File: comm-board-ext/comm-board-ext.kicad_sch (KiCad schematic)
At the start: 39 parts, among them J1 GND, J10 MCU-RxD1, J11 MCU-TxD2, J12 MCU-RxD2, J2 GND, J3 +5V, J4 +3.3V, J5 D1-, J6 D1+, J7 D2+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

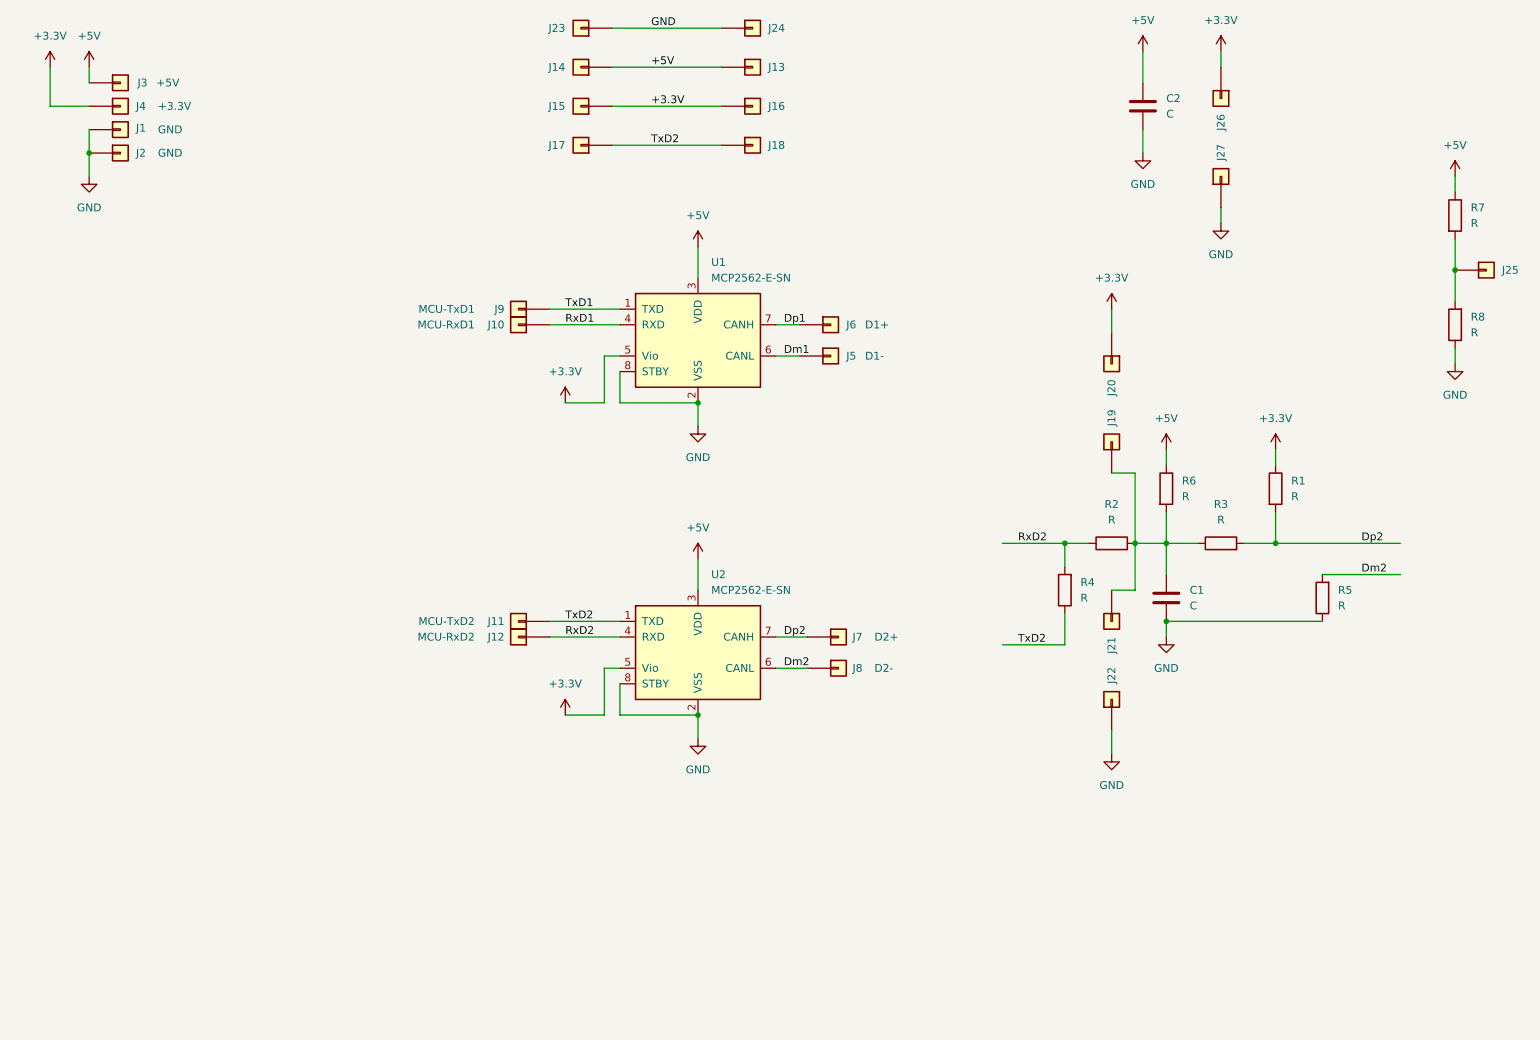
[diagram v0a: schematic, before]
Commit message: comm-board-ext: Modified for CNC milling
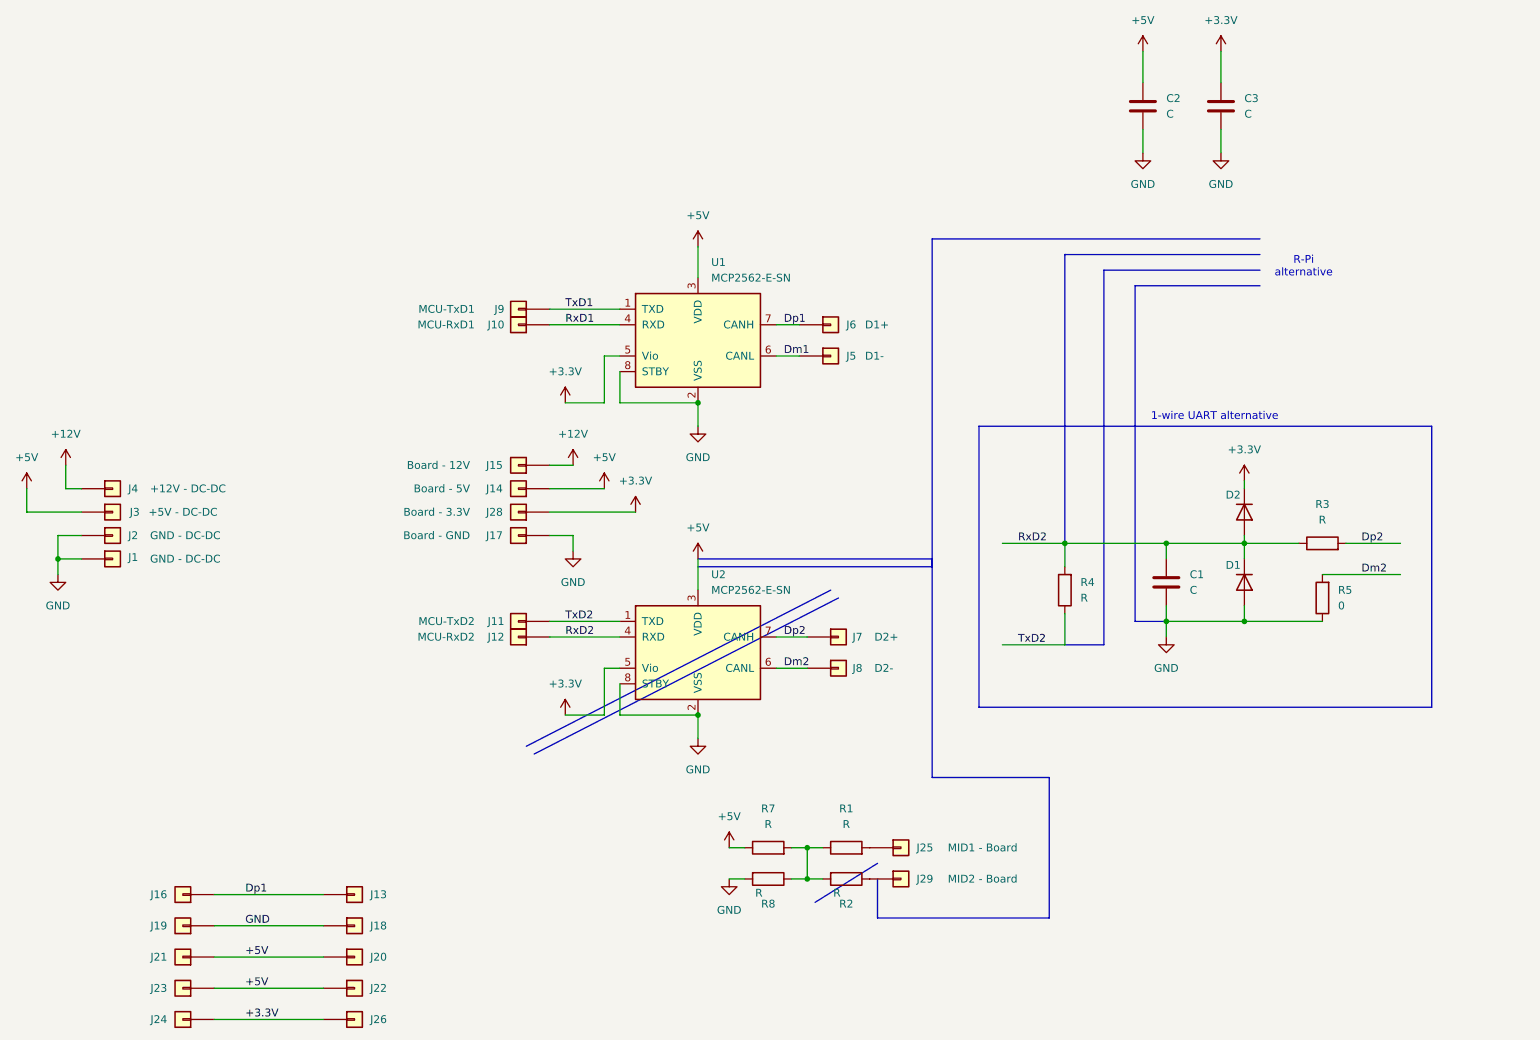
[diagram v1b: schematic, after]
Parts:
- removed J27: ~, Footprints:VHDR, symbol Connector_Generic:Conn_01x01
- removed R6: R, Resistor_SMD:R_1206_3216Metric_Pad1.30x1.75mm_HandSolder, symbol Device:R
- added C3: C, Footprints:CNC-mill-0.7-CAP, symbol Device:C
- added D1, D2: D, Footprints:CNC-mill-0.7-RES, symbol Device:D
- added J28: Board - 3.3V, Footprints:CHDR, symbol Connector_Generic:Conn_01x01
- added J29: MID2 - Board, Footprints:CHDR, symbol Connector_Generic:Conn_01x01
- C1, C2: footprint Resistor_SMD:R_1206_3216Metric_Pad1.30x1.75mm_HandSolder -> Footprints:CNC-mill-0.7-CAP
- J1, J2: value GND -> GND - DC-DC; footprint Footprints:BBHDR -> Footprints:CHDR
- J10, J11, J12, J5, J6, J7, J8, J9: footprint Footprints:BBHDR -> Footprints:CHDR
- J14: value ~ -> Board - 5V; footprint Footprints:VHDR -> Footprints:CHDR
- J15: value ~ -> Board - 12V; footprint Footprints:VHDR -> Footprints:CHDR
- J17: value ~ -> Board - GND; footprint Footprints:VHDR -> Footprints:CHDR
- J19, J20, J21, J22: footprint Footprints:CHDR -> Footprints:VHDR
- J25: value ~ -> MID1 - Board; footprint Footprints:VHDR -> Footprints:CHDR
- J3: value +5V -> +5V - DC-DC; footprint Footprints:BBHDR -> Footprints:CHDR
- J4: value +3.3V -> +12V - DC-DC; footprint Footprints:BBHDR -> Footprints:CHDR
- R1, R2, R3, R4, R7, R8: footprint Resistor_SMD:R_1206_3216Metric_Pad1.30x1.75mm_HandSolder -> Footprints:CNC-mill-0.7-RES
- R5: value R -> 0; footprint Resistor_SMD:R_1206_3216Metric_Pad1.30x1.75mm_HandSolder -> Footprints:CNC-mill-0.7-RES
- U1, U2: footprint Package_SO:SOIC-8_3.9x4.9mm_P1.27mm -> Footprints:CNC-mill-0.7-DIP-8
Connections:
- net +3.3V: now also J24.1 (Pin_1), C3.1, D2.1 (K), J28.1 (Pin_1); no longer J15.1 (Pin_1), J16.1 (Pin_1), J20.1 (Pin_1), J4.1 (Pin_1), R1.1
- net +5V: now also J20.1 (Pin_1), J21.1 (Pin_1), J22.1 (Pin_1), J23.1 (Pin_1); no longer J13.1 (Pin_1)
- net Dp1: now also J13.1 (Pin_1), J16.1 (Pin_1)
- net Dp2: no longer R1.2
- net GND: now also J17.1 (Pin_1), J18.1 (Pin_1), J19.1 (Pin_1), R8.2, C3.2, D1.2 (A); no longer J22.1 (Pin_1), J23.1 (Pin_1), J24.1 (Pin_1), R8.1
- net RxD2: now also C1.1, R3.1, D1.1 (K), D2.2 (A); no longer R2.1
- net TxD2: no longer J17.1 (Pin_1), J18.1 (Pin_1)
- new net: J29.1 (Pin_1), R2.1
- new net: R1.1, R2.2, R7.2, R8.1
- new net: J25.1 (Pin_1), R1.2
- new net +12V: J15.1 (Pin_1), J4.1 (Pin_1)
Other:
- note added: "1-wire UART alternative"
- note added: "R-Pi alternative"
- moved on the sheet: C1, J1, J14, J2, J25, J3, J4, R3, R7, R8
